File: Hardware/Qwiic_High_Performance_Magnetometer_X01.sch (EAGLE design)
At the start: 28 parts, among them J1 Qwiic, J2 Qwiic, U1 MMC5893MA_QFN16

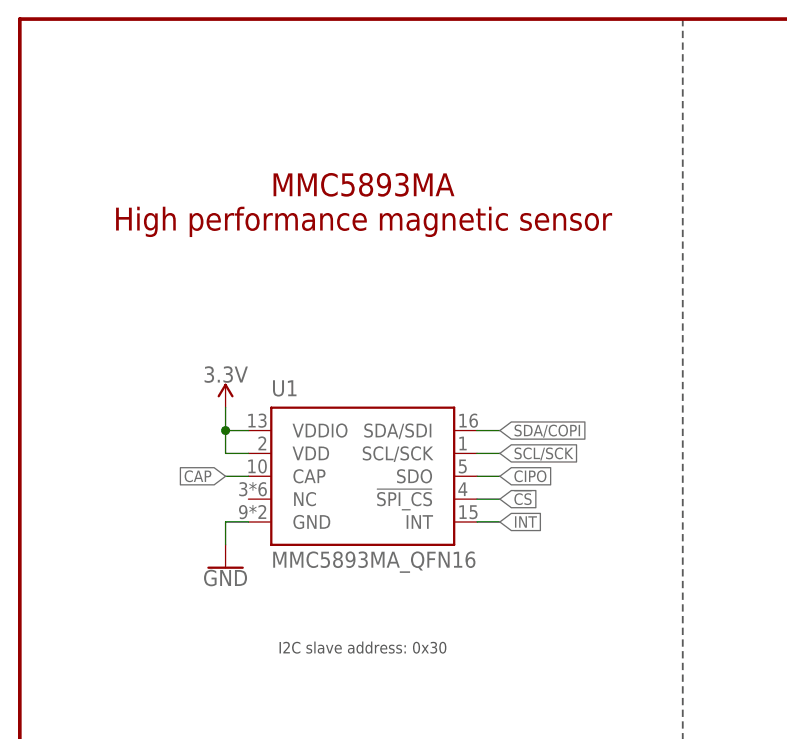
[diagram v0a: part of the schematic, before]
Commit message: Fixed typo
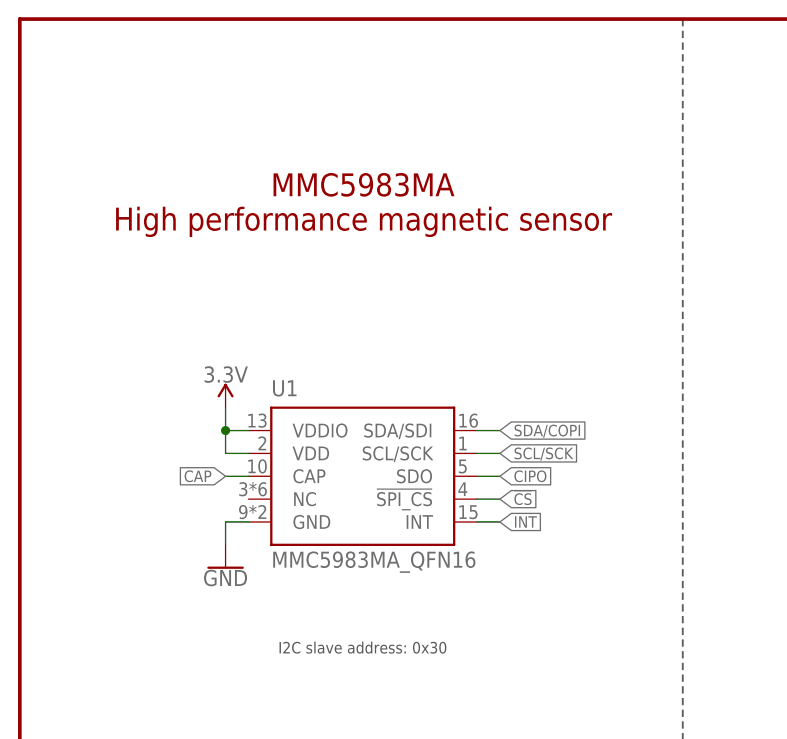
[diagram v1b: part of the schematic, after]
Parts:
- U1: value MMC5893MA_QFN16 -> MMC5983MA_QFN16; device SparkFun-Sensors:MMC5893MA_QFN16 -> SparkFun-Sensors:MMC5983MA_QFN16
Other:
- note added: "MMC5983MA High performance magnetic sensor"
- note removed: "MMC5893MA High performance magnetic sensor"
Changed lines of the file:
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@@
 <part name="C2" library="SparkFun-Capacitors" deviceset="10UF" device="-0603-6.3V-20%" value="10uF"/>
 <part name="GND4" library="SparkFun-PowerSymbols" deviceset="GND" device=""/>
-<part name="U1" library="SparkFun-Sensors" deviceset="MMC5893MA" device="_QFN16"/>
+<part name="U1" library="SparkFun-Sensors" deviceset="MMC5983MA" device="_QFN16"/>
 <part name="SUPPLY2" library="SparkFun-PowerSymbols" deviceset="3.3V" device=""/>
 <part name="GND7" library="SparkFun-PowerSymbols" deviceset="GND" device=""/>
@@
 <text x="38.1" y="88.9" size="2.54" layer="94" align="center">Power decoupling</text>
 <wire x1="0" y1="48.26" x2="0" y2="50.8" width="0.2032" layer="97" style="longdash"/>
-<text x="38.1" y="165.1" size="2.54" layer="94" align="center">MMC5893MA
+<text x="38.1" y="165.1" size="2.54" layer="94" align="center">MMC5983MA
 High performance magnetic sensor</text>
 <text x="38.1" y="115.57" size="1.27" layer="97" align="center">I2C slave address: 0x30</text>
